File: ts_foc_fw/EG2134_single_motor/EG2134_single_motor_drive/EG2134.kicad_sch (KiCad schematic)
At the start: 33 parts, among them Q1 RU3089M-C, Q2 RU3089M-C, Q3 RU3089M-C, Q4 RU3089M-C, Q5 RU3089M-C, Q6 RU3089M-C, U3 EG2134_N

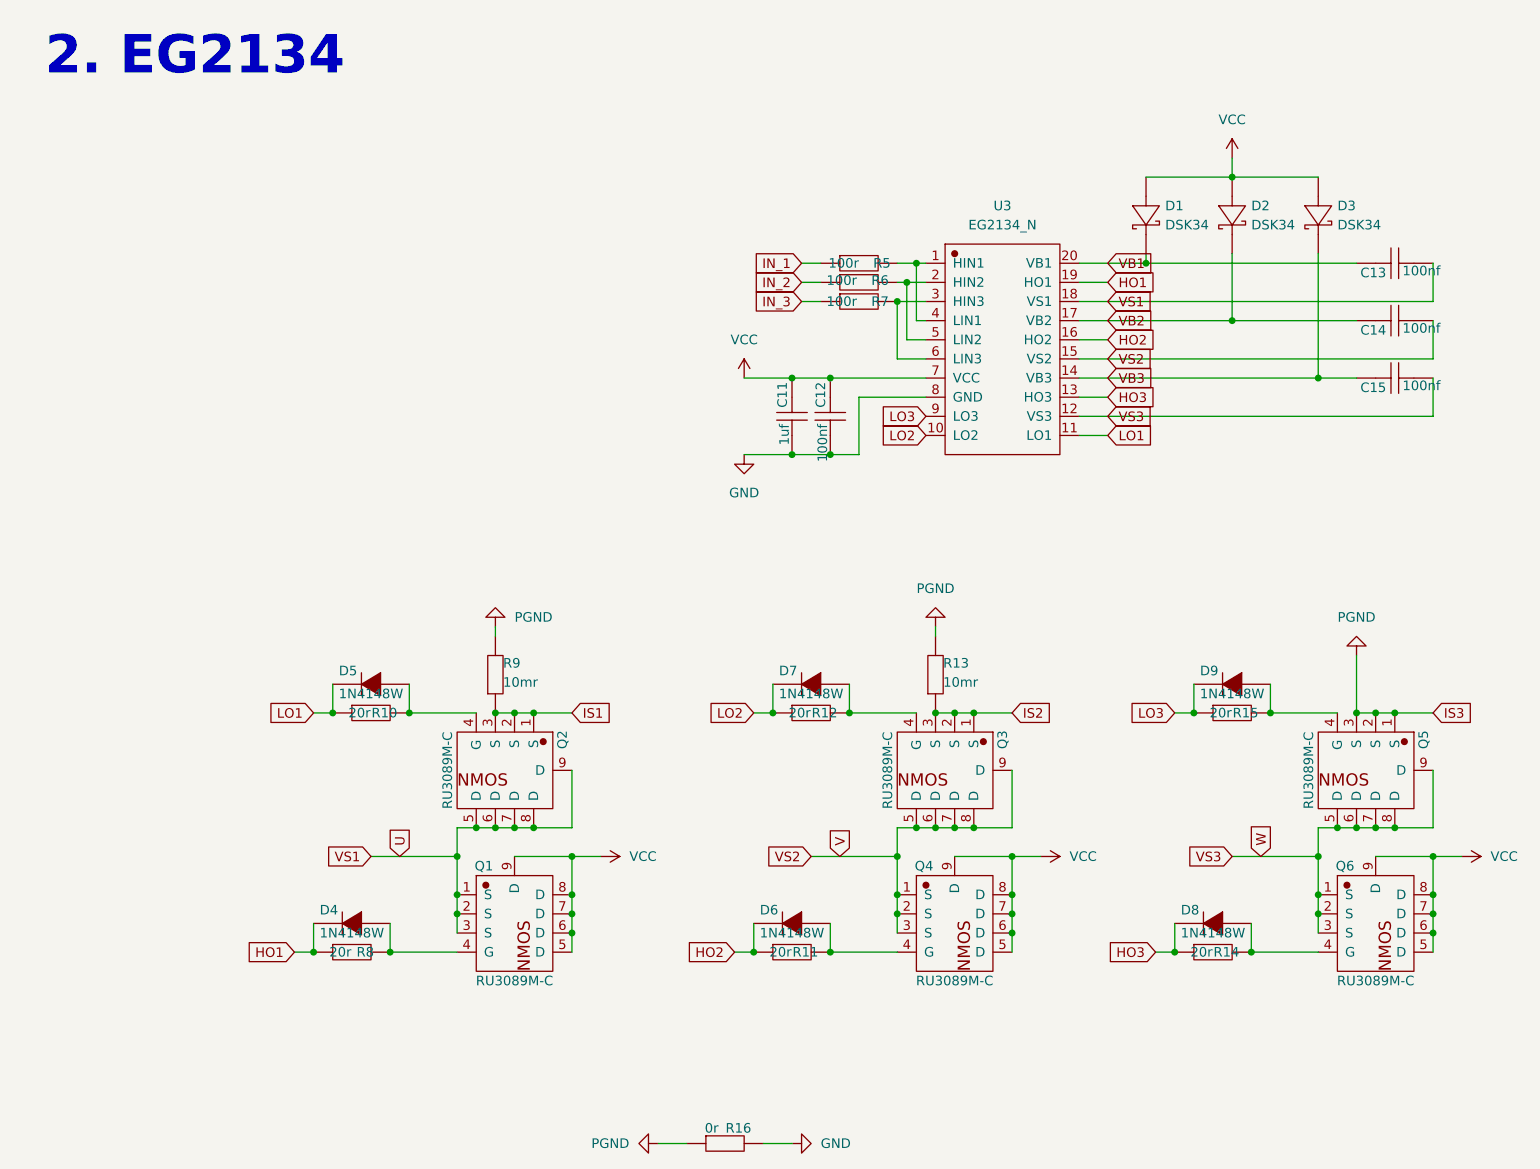
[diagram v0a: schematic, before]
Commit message: PCB布局完成，等待布线
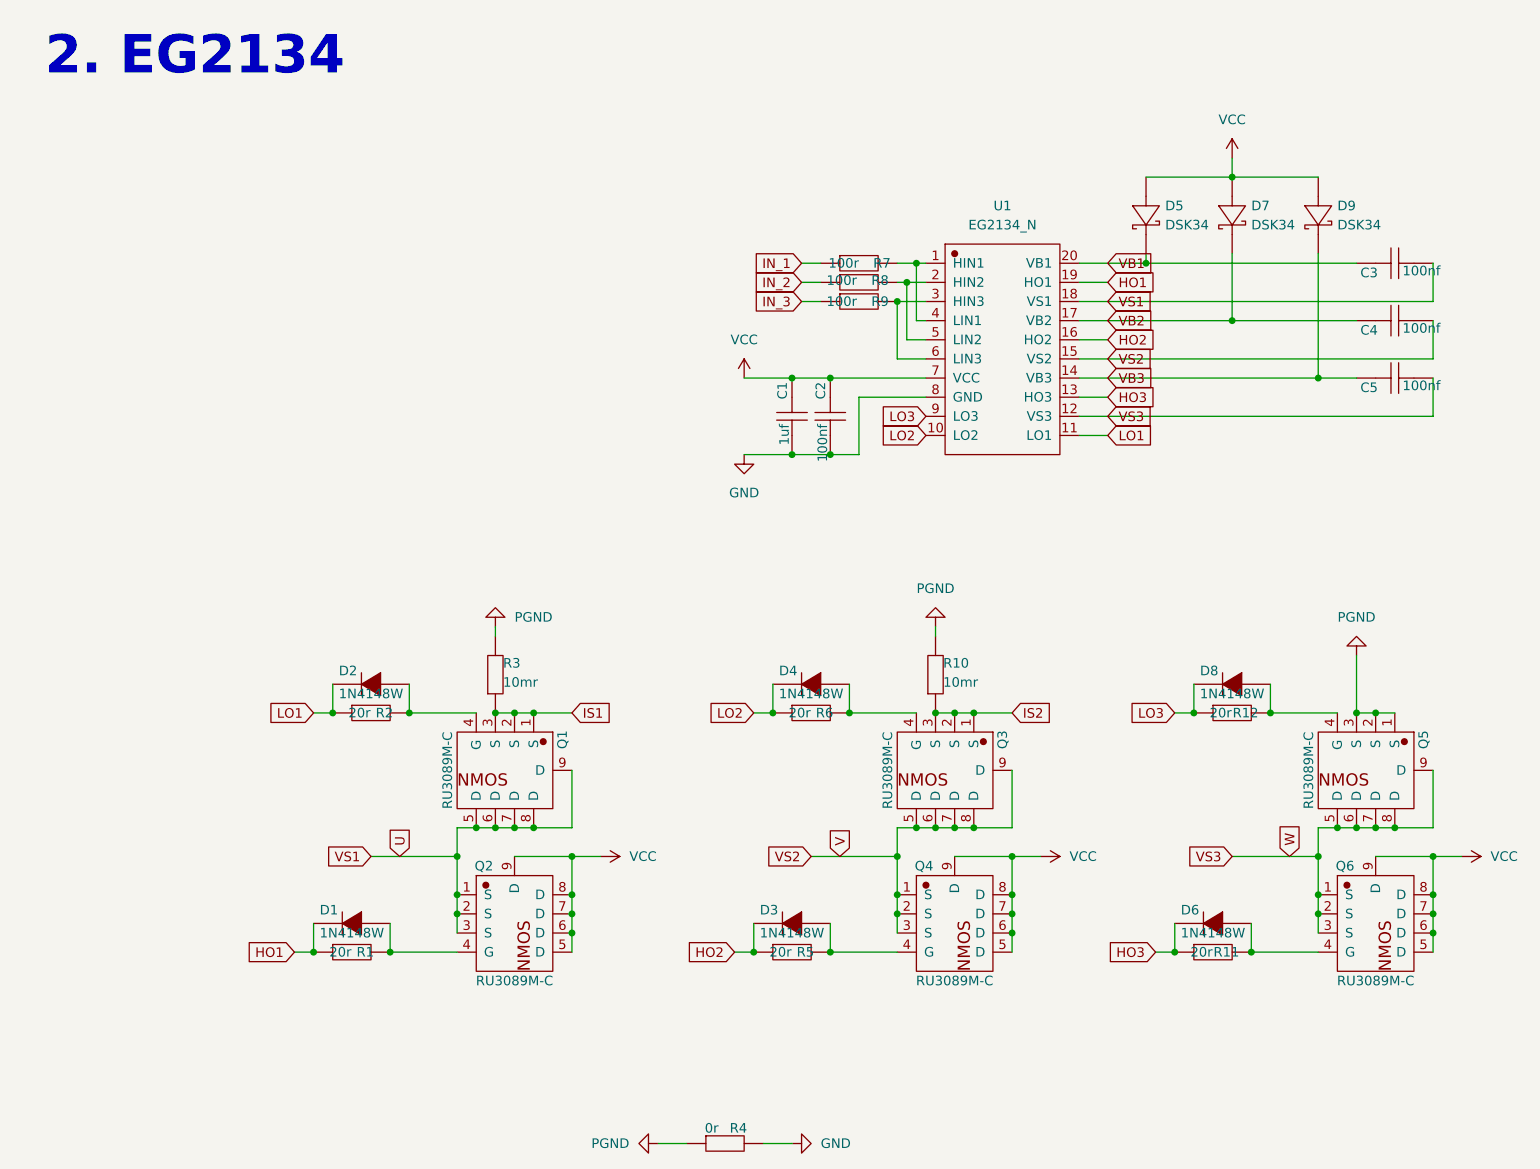
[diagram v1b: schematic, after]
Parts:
- renumbered C11 to C1, C12 to C2, C13 to C3, C14 to C4, C15 to C5, D4 to D1, D5 to D2, D6 to D3, D7 to D4, D1 to D5, D8 to D6, D2 to D7, D9 to D8, D3 to D9, Q2 to Q1, Q1 to Q2, R8 to R1, R13 to R10, R14 to R11, R15 to R12, R10 to R2, R9 to R3, R16 to R4, R11 to R5, R12 to R6, R5 to R7, R6 to R8, R7 to R9, U3 to U1
